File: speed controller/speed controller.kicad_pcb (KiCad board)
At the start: 2 copper layers, 16 parts, among them Q1 IQE022N06LM5CG, Q2 IQE022N06LM5CG, Q3 IQE022N06LM5CG, Q4 IQE022N06LM5CG, Q5 IQE022N06LM5CG, Q6 IQE022N06LM5CG, U1 DRV8323RSRGZT, U2 STM32F405RGTx, U3 TPS62162DSG, U4 TJA1051TK-3

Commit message: inital board layout
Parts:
- added C15: 2.2u, Capacitor_SMD:C_0603_1608Metric, F.Cu at (202.8, 87.8)
- added C16: 2.2u, Capacitor_SMD:C_0603_1608Metric, F.Cu at (213.0, 95.0)
- added C17: 100n, Capacitor_SMD:C_0402_1005Metric, F.Cu at (212.5, 99.2)
- added C18: 2.2u, Capacitor_SMD:C_0603_1608Metric, F.Cu at (196.2, 88.5)
- added C19: 100n, Capacitor_SMD:C_0402_1005Metric, F.Cu at (199.2, 89.0)
- added C2: 10u, Capacitor_SMD:C_0402_1005Metric, F.Cu at (180.2, 89.5)
- added C20: 100n, Capacitor_SMD:C_0402_1005Metric, F.Cu at (212.8, 92.2)
- added C21: 100n, Capacitor_SMD:C_0402_1005Metric, F.Cu at (197.2, 99.0)
- added C22: 100n, Capacitor_SMD:C_0402_1005Metric, F.Cu at (209.0, 103.2)
- added C23: 1u, Capacitor_SMD:C_0603_1608Metric, F.Cu at (210.0, 104.8)
- added C24: 4.7u, Capacitor_SMD:C_0402_1005Metric, F.Cu at (197.7, 102.0)
- added C25: 1u, Capacitor_SMD:C_1206_3216Metric, F.Cu at (183.0, 102.0)
- added C26: 0.1u, Capacitor_SMD:C_0603_1608Metric, F.Cu at (180.5, 102.0)
- added C27: 10u, Capacitor_SMD:C_1210_3225Metric, F.Cu at (177.5, 102.0)
- added C28: 47n, Capacitor_SMD:C_0603_1608Metric, F.Cu at (183.2, 97.8)
- added C29: 10u, Capacitor_SMD:C_0402_1005Metric, F.Cu at (180.2, 91.8)
- added C3: 22u, Capacitor_SMD:C_0603_1608Metric, F.Cu at (201.5, 85.0)
- added C30: 100n, Capacitor_SMD:C_0603_1608Metric, F.Cu at (193.5, 96.2)
- added C31: 2.2u, Capacitor_SMD:C_1206_3216Metric, F.Cu at (178.8, 97.8)
- added C32: 2.2u, Capacitor_SMD:C_0603_1608Metric, F.Cu at (192.8, 92.5)
- added C33: 2.2u, Capacitor_SMD:C_0603_1608Metric, F.Cu at (211.7, 108.0)
- added C34: 10p, Capacitor_SMD:C_0402_1005Metric, F.Cu at (202.0, 103.0)
- added C35: 100n, Capacitor_SMD:C_0402_1005Metric, F.Cu at (207.0, 106.5)
- added C36: 10p, Capacitor_SMD:C_0402_1005Metric, F.Cu at (204.2, 103.0)
- added C37: 100n, Capacitor_SMD:C_0402_1005Metric, F.Cu at (195.5, 105.0)
- added C4: 10u, Capacitor_SMD:C_0402_1005Metric, F.Cu at (196.5, 84.2)
- added J1: ~, TestPoint:TestPoint_THTPad_2.0x2.0mm_Drill1.0mm, F.Cu at (190.2, 119.0)
- added J2: ~, TestPoint:TestPoint_THTPad_2.0x2.0mm_Drill1.0mm, F.Cu at (195.5, 119.0)
- added J3: ~, TestPoint:TestPoint_THTPad_2.0x2.0mm_Drill1.0mm, F.Cu at (200.2, 119.0)
- added J5: Conn_02x05_Counter_Clockwise, Connector_PinHeader_1.27mm:PinHeader_2x05_P1.27mm_Vertical, F.Cu at (178.4, 109.0)
- added L1: 22u, Inductor_SMD:DR74, F.Cu at (187.5, 88.0)
- added L2: 2.2u, Inductor_SMD:L_1008_2520Metric, F.Cu at (204.0, 84.8)
- added R10: 1m, Resistor_SMD:R_0805_2012Metric, F.Cu at (204.6, 109.0)
- added R11: 39k, Resistor_SMD:R_01005_0402Metric, F.Cu at (191.0, 116.8)
- added R12: 2.2k, Resistor_SMD:R_01005_0402Metric, F.Cu at (189.2, 116.8)
- added R13: 10k, Resistor_SMD:R_0402_1005Metric, F.Cu at (195.8, 103.3)
- added R14: 39k, Resistor_SMD:R_01005_0402Metric, F.Cu at (194.5, 116.8)
- added R15: 10k, Resistor_SMD:R_0402_1005Metric, F.Cu at (180.0, 94.2)
- added R16: 39k, Resistor_SMD:R_01005_0402Metric, F.Cu at (199.2, 116.8)
- added R17: 2.2k, Resistor_SMD:R_01005_0402Metric, F.Cu at (201.0, 116.8)
- added R18: 2.2k, Resistor_SMD:R_01005_0402Metric, F.Cu at (196.2, 116.8)
- added R5: 54.9k, Resistor_SMD:R_0402_1005Metric, F.Cu at (182.0, 94.8)
- added R6: 100k, Resistor_SMD:R_0402_1005Metric, F.Cu at (178.0, 91.7)
- added R7: 100k, Resistor_SMD:R_0402_1005Metric, F.Cu at (200.8, 82.0)
- added R8: 1m, Resistor_SMD:R_0805_2012Metric, F.Cu at (186.5, 109.2)
- added R9: 1m, Resistor_SMD:R_0805_2012Metric, F.Cu at (195.0, 109.0)
- added Y1: ECS-80-8-33-JGN-TR3, Inductor_SMD:ECS-80-8-33-JGN-TR3, F.Cu at (203.1, 105.4)
- h1: moved to B.Cu
- moved Q5 105.8 mm to (202.4, 112.9)
- moved Q6 105.8 mm to (206.5, 112.9), turned to 180 degrees
- moved Q3 103.2 mm to (197.4, 113.0)
- moved Q4 100.8 mm to (193.0, 113.1), turned to 180 degrees
- moved Q2 98.2 mm to (187.7, 113.0), turned to 180 degrees
- moved Q1 98.2 mm to (183.6, 113.0)
- moved P1 75.4 mm to (185.0, 118.5), turned to 90 degrees
- moved U2 74.2 mm to (205.0, 95.5), turned to 90 degrees
- moved U3 73.8 mm to (199.0, 84.1)
- moved R2 73.4 mm to (213.2, 103.5)
- moved R3 73.3 mm to (213.2, 104.5), turned to 180 degrees
- moved D1 67.8 mm to (193.5, 84.0), turned to -90 degrees
- moved U1 64.9 mm to (189.7, 102.0), turned to 0 degrees
- moved D3 60.9 mm to (187.8, 95.0), turned to 180 degrees
- moved h1 53.0 mm to (195.0, 100.4), turned to -90 degrees
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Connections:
- U2 pad 15: /STM32F405RGTx/VOLTAGE_A -> /STM32F405RGTx/VOLTAGE_B
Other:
- board outline added: 41.3 x 41.3 mm

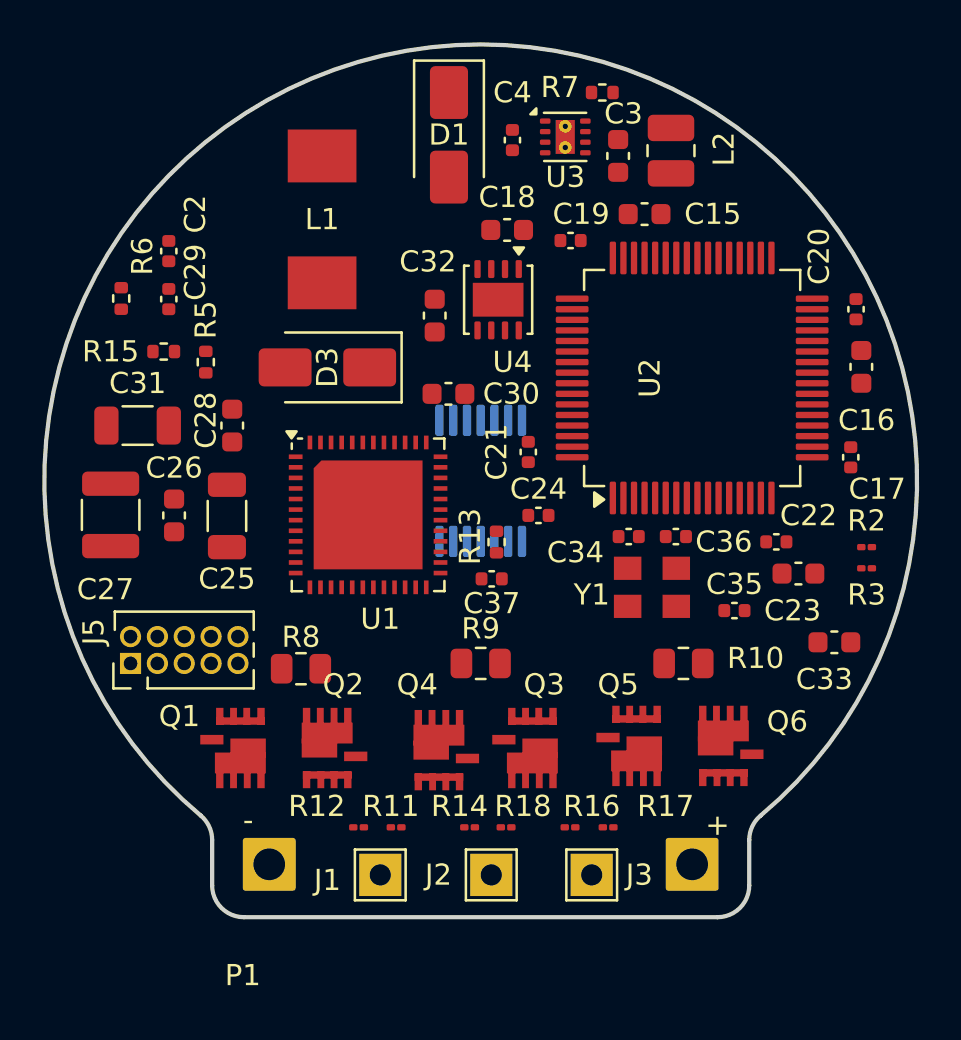
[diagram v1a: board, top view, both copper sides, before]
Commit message: design rules JLCPCB, and started trace routing
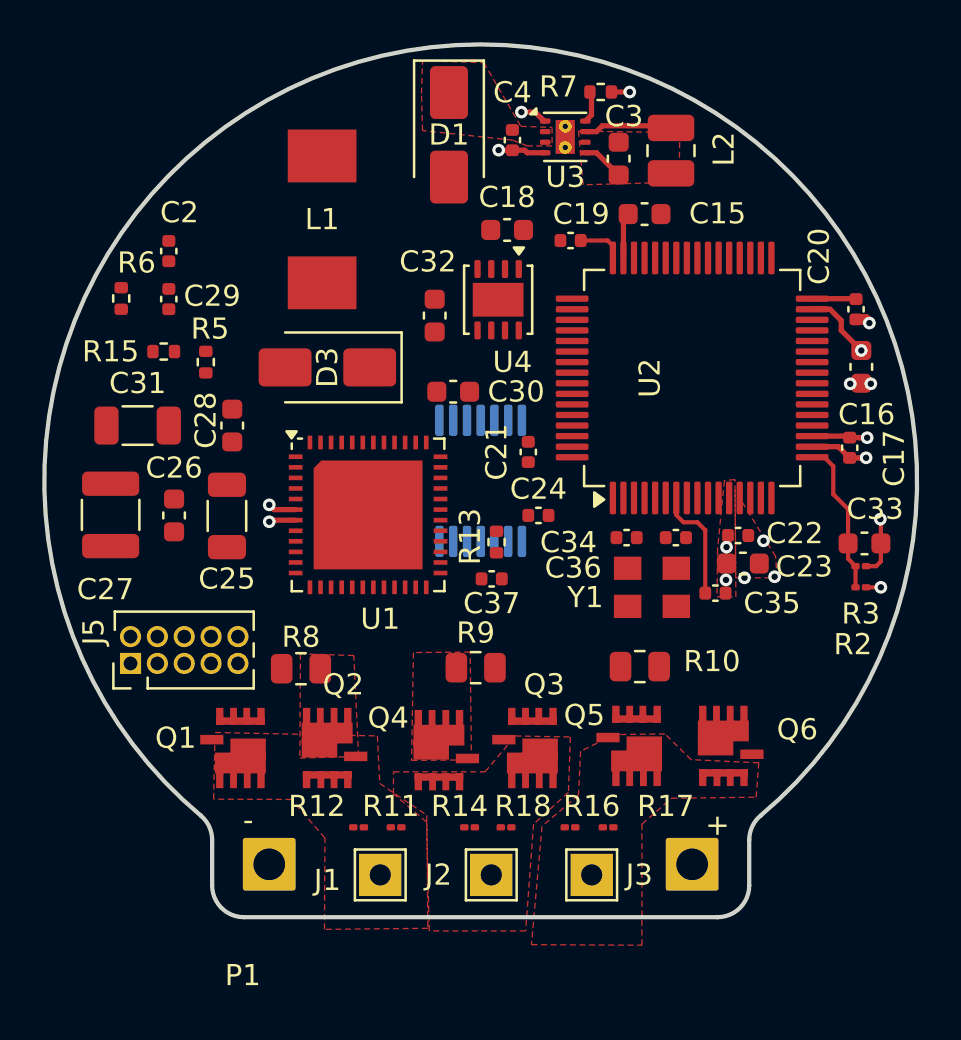
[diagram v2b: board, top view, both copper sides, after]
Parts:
- moved C33 4.89 mm to (213.2, 103.3), turned to 0 degrees
- moved C23 2.67 mm to (207.4, 104.3)
- moved R10 2.07 mm to (202.5, 109.2)
- moved C22 1.83 mm to (207.2, 103.0)
- moved C35 1.22 mm to (206.1, 105.7)
- moved R2 0.94 mm to (213.0, 104.4)
- moved R3 0.94 mm to (213.0, 105.4)
- moved C17 0.45 mm to (212.4, 98.8)
- moved R9 0.31 mm to (194.8, 109.2)
- moved C30 0.25 mm to (193.7, 96.2)
- moved C3 0.13 mm to (201.5, 85.1)
- moved C34 0.11 mm to (201.9, 103.0)
- moved R7 0.08 mm to (200.7, 82.0)
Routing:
- net GND: track 0.00 -> 12.8 mm, vias 0 -> 9
- net +3.3V: track 0.00 -> 8.48 mm, vias 0 -> 6
- net /STM32F405RGTx/ADC_TEMP: track 0.00 -> 7.34 mm
- net Net-(U2-VCAP_1): track 0.00 -> 5.57 mm, vias 0 -> 1
- net /STM32F405RGTx/NRST: track 0.00 -> 5.45 mm
- net Net-(U3-SW): track 0.00 -> 4.06 mm
- net +BATT: track 0.00 -> 2.62 mm, vias 0 -> 2
- net /STM32F405RGTx/PG: track 0.00 -> 1.47 mm
- added copper zone on F.Cu, net +3.3V
- added copper zone on F.Cu, net +5V
- added copper zone on F.Cu, net /DRV8323RSRGZT/SPA
- added copper zone on F.Cu, net /DRV8323RSRGZT/SPB
- added copper zone on F.Cu, net /drive/phase_A
- added copper zone on F.Cu, net /drive/phase_B
- added copper zone on F.Cu, net /drive/phase_C
- added copper zone on F.Cu, net GND
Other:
- copper layers 2 -> 4

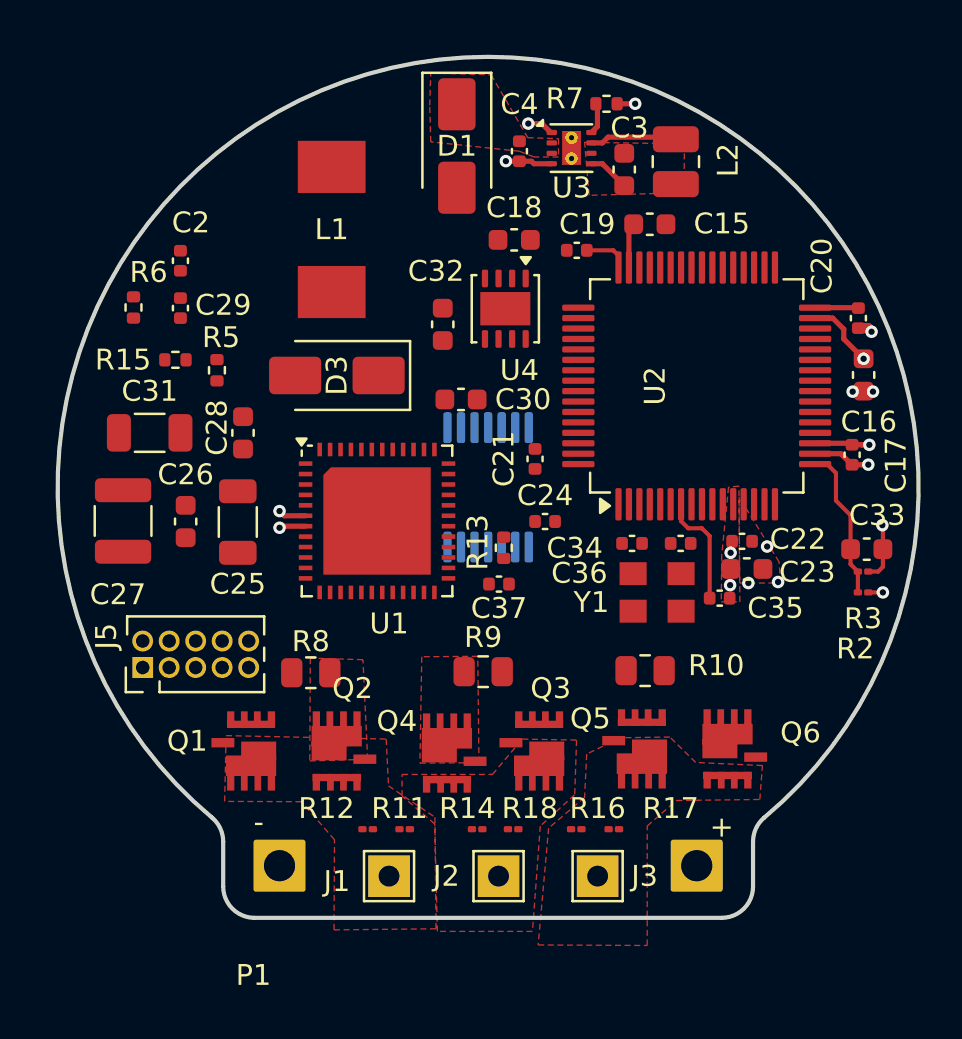
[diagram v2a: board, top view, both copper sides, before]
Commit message: trace routing. needs more work on 5v bus. prelem layout complete
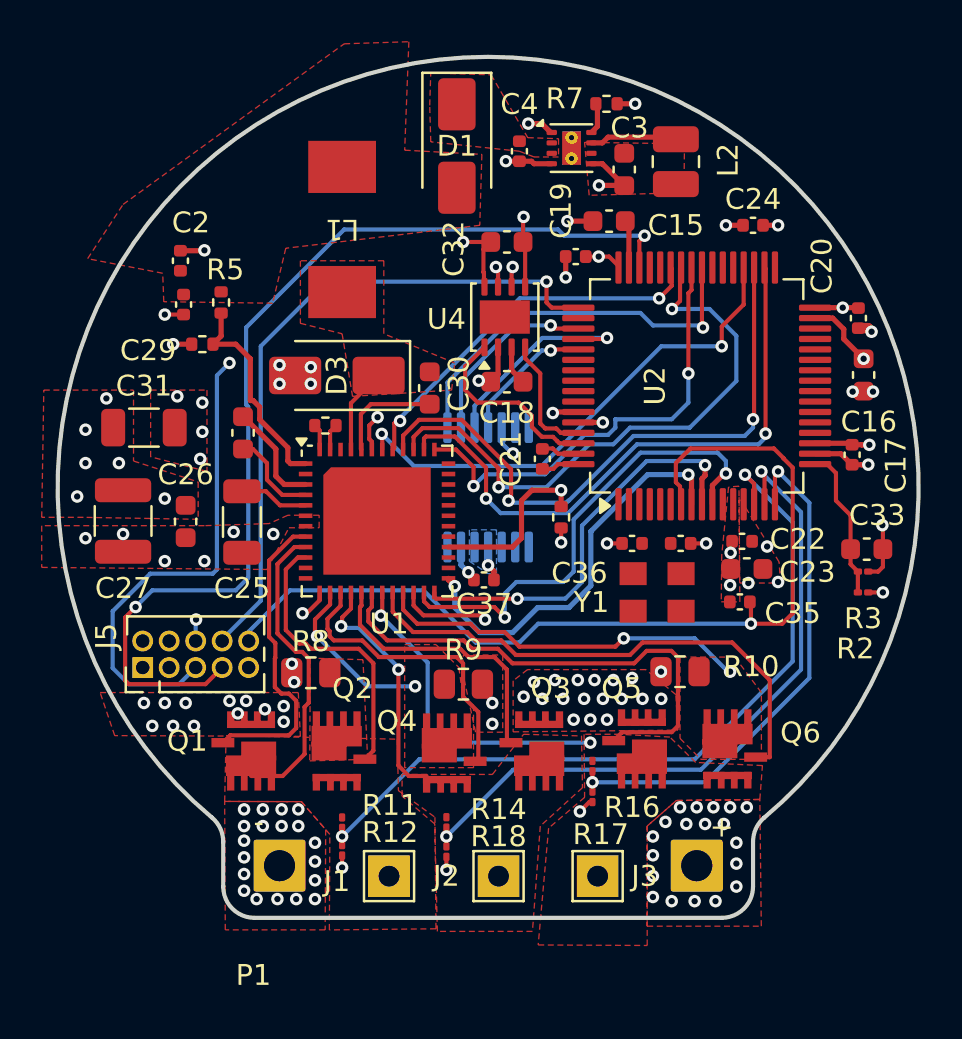
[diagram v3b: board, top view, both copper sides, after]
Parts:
- moved C24 17.4 mm to (207.7, 87.8)
- moved R6 10.8 mm to (187.2, 97.4), turned to 180 degrees
- moved C18 6.81 mm to (195.9, 95.3), turned to 180 degrees
- moved C32 5.01 mm to (195.9, 88.6), turned to 180 degrees
- moved R18 3.38 mm to (193.0, 117.8), turned to -90 degrees
- moved R5 3.26 mm to (182.2, 91.5)
- moved R16 3.12 mm to (200.0, 113.7), turned to -90 degrees
- moved R13 3.11 mm to (198.5, 101.8)
- moved R11 3.02 mm to (188.0, 116.4), turned to -90 degrees
- moved C15 1.96 mm to (200.8, 87.6), turned to 180 degrees
- moved R17 1.86 mm to (200.0, 115.2), turned to -90 degrees
- moved R10 1.68 mm to (204.2, 109.2)
- moved C30 1.60 mm to (192.2, 95.6), turned to 90 degrees
- moved R12 1.59 mm to (188.0, 117.8), turned to -90 degrees
- moved R14 1.51 mm to (193.0, 116.4), turned to -90 degrees
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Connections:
- C15 pad 1: Net-(U2-VCAP_1) -> Net-(U2-VCAP_2)
- U2 pad 47: Net-(U2-VCAP_1) -> Net-(U2-VCAP_2)
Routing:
- net /STM32F405RGTx/SWDIO: track 0.00 -> 49.6 mm, vias 0 -> 2
- net /STM32F405RGTx/NRST: track 5.45 -> 49.2 mm, vias 0 -> 1
- net /STM32F405RGTx/VOLTAGE_A: track 0.00 -> 37.4 mm, vias 0 -> 2
- net GND: track 12.8 -> 48.8 mm, vias 9 -> 64
- net /STM32F405RGTx/VOLTAGE_B: track 0.00 -> 33.1 mm, vias 0 -> 2
- net /STM32F405RGTx/SWCLK: track 0.00 -> 32.5 mm, vias 0 -> 1
- net +3.3V: track 8.48 -> 40.5 mm, vias 6 -> 13
- net /DRV8323RSRGZT/INLB: track 0.00 -> 29.6 mm, vias 0 -> 2
- net /DRV8323RSRGZT/INLA: track 0.00 -> 29.0 mm, vias 0 -> 2
- net /DRV8323RSRGZT/INHB: track 0.00 -> 28.0 mm, vias 0 -> 2
- net /STM32F405RGTx/VOLTAGE_C: track 0.00 -> 25.6 mm, vias 0 -> 2
- net /DRV8323RSRGZT/GLC: track 0.00 -> 25.2 mm
- net /DRV8323RSRGZT/INLC: track 0.00 -> 24.3 mm, vias 0 -> 2
- net /DRV8323RSRGZT/GHC: track 0.00 -> 24.2 mm
- net /DRV8323RSRGZT/SOC: track 0.00 -> 23.2 mm, vias 0 -> 2
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- added copper zone on B.Cu, net +3.3V
- added copper zone on In2.Cu, net +3.3V
- added copper zone on F.Cu, net +BATT
- added copper zone on In2.Cu, net +BATT
- added copper zone on F.Cu, net /DRV8323RSRGZT/SPC
- added copper zone on In1.Cu, net GND
- added copper zone on F.Cu, net Net-(D1-A)
- added copper zone on F.Cu, net Net-(D3-K)
